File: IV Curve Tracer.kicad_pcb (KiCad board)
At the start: 2 copper layers, 159.4 x 80.1 mm, 61 parts, among them IC1 MAX680ESA+, J0 TB002-500-02BE, J1 CAN_Out, J5 Conn_01x15, J6 Conn_01x15, Q1 IRF100P218XKMA1, Q2 IRF100P218XKMA1, SW0 SW_Rotary2x3, U1 INA211CQDCKRQ1, U2 LT1215, U3 LT1215, U4 ADM3055E, U5 CDSOT23-T24CAN

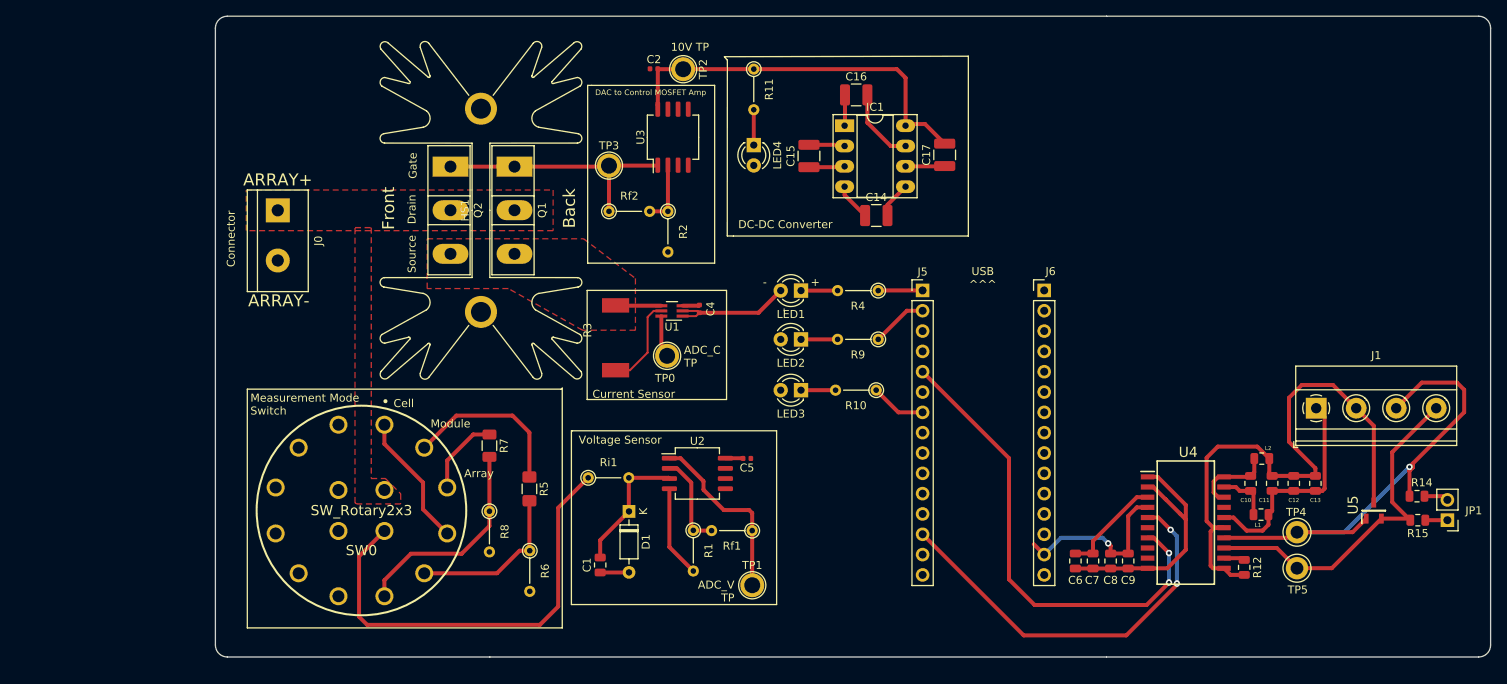
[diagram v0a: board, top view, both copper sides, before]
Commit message: CAN updated, needs bugfixes and footprint review.
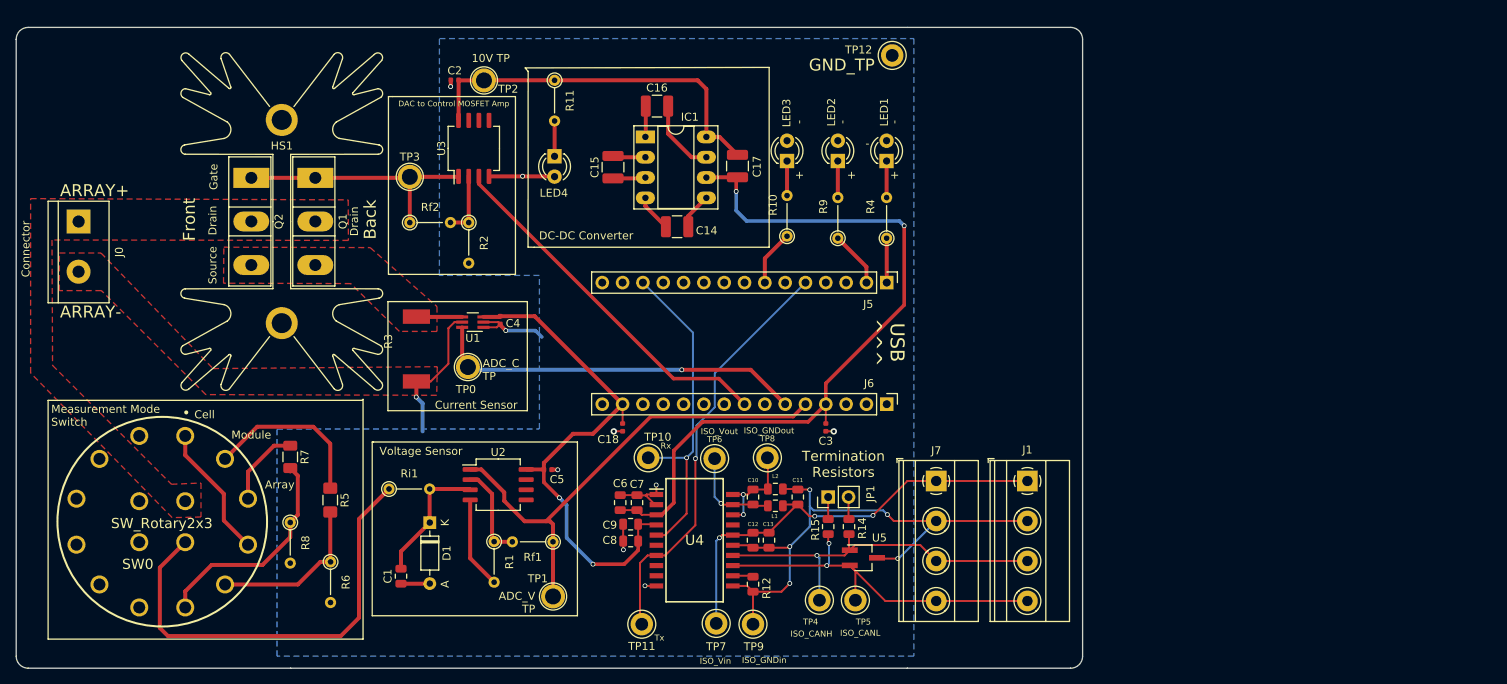
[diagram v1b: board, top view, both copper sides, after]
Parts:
- added C18: .1uF, Capacitor_SMD:C_0402_1005Metric, F.Cu at (171.5, 131.4)
- added C3: .1uF, Capacitor_SMD:C_0402_1005Metric, F.Cu at (196.9, 131.4)
- added J7: CAN_In, TerminalBlock_Phoenix:TerminalBlock_Phoenix_MKDS-1,5-4_1x04_P5.00mm_Horizontal, F.Cu at (210.7, 138.1)
- added TP10: CAN_Rx, TestPoint:TestPoint_Keystone_5005-5009_Compact, F.Cu at (174.7, 135.2)
- added TP11: CAN_Tx, TestPoint:TestPoint_Keystone_5005-5009_Compact, F.Cu at (173.9, 156.0)
- added TP12: GroundTP, TestPoint:TestPoint_Keystone_5005-5009_Compact, F.Cu at (205.2, 84.9)
- added TP6: ISO_Vout, TestPoint:TestPoint_Keystone_5005-5009_Compact, F.Cu at (183.0, 135.3)
- added TP7: ISO_Vin, TestPoint:TestPoint_Keystone_5005-5009_Compact, F.Cu at (183.2, 155.9)
- added TP8: ISO_GNDout, TestPoint:TestPoint_Keystone_5005-5009_Compact, F.Cu at (189.6, 135.2)
- added TP9: ISO_GNDin, TestPoint:TestPoint_Keystone_5005-5009_Compact, F.Cu at (187.8, 156.0)
- U5: footprint SamacSys_Parts:SOT95P230X117-3N -> Package_TO_SOT_SMD:SOT-23W_Handsoldering
- moved JP1 77.5 mm to (197.2, 140.1), turned to 90 degrees
- moved R15 73.7 mm to (197.2, 143.8), turned to 270 degrees
- moved R14 71.1 mm to (199.8, 143.8), turned to 270 degrees
- moved C13 68.7 mm to (189.8, 145.5), turned to 270 degrees
- moved C12 68.0 mm to (187.8, 145.5), turned to 270 degrees
- moved U5 64.1 mm to (201.6, 147.7), turned to 0 degrees
- moved C9 62.4 mm to (172.5, 143.5), turned to 180 degrees
- moved C10 62.2 mm to (187.8, 140.1)
- moved U4 61.4 mm to (180.5, 145.5)
- moved R12 61.4 mm to (187.8, 151.0)
- moved L2 60.9 mm to (190.6, 139.1)
- moved L1 60.7 mm to (190.6, 141.2)
- moved TP4 60.3 mm to (196.1, 153.0)
- moved C8 60.0 mm to (172.5, 145.6), turned to 180 degrees
- moved C11 59.3 mm to (193.4, 140.1)
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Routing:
- net +5V: track 17.8 -> 94.2 mm, vias 0 -> 2
- net DAC_Control: track 0.00 -> 45.6 mm
- net ADC_C: track 5.26 -> 46.8 mm, vias 0 -> 1
- net +3V3: track 26.5 -> 66.7 mm, vias 1 -> 2
- net ADC_V: track 22.8 -> 61.3 mm
- net Net-(C11-Pad1): track 28.1 -> 55.4 mm, vias 0 -> 3
- net /CAN_H: track 63.7 -> 46.0 mm
- net CAN_RX: track 50.4 -> 41.5 mm, vias 2 -> 1
- net CAN_TX: track 60.1 -> 52.6 mm, vias 2 -> 1
- net GND: track 79.9 -> 73.3 mm, vias 0 -> 10
- net Net-(C10-Pad1): track 6.64 -> 11.9 mm, vias 0 -> 1
- net /CAN_L: track 44.2 -> 47.4 mm, vias 0 -> 2
- net Net-(C10-Pad2): track 10.2 -> 12.5 mm, vias 0 -> 2
- net Net-(R7-Pad2): track 26.6 -> 27.9 mm
- net +10V: track 48.5 -> 47.6 mm
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- added copper zone on B.Cu, net GND
- added copper zone on F.Cu, net GND
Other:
- board size 159.4 x 80.1 mm -> 133.3 x 80.1 mm
- board text added: "A"
- board text added: "GND_TP"
- board text added: "ISO_CANH"
- board text added: "ISO_CANL"
- board text added: "ISO_GNDin"
- board text added: "ISO_GNDout"
- board text added: "ISO_Vin"
- board text added: "ISO_Vout"
- board text added: "Rx"
- board text added: "Termination Resistors"
- board text added: "Tx"

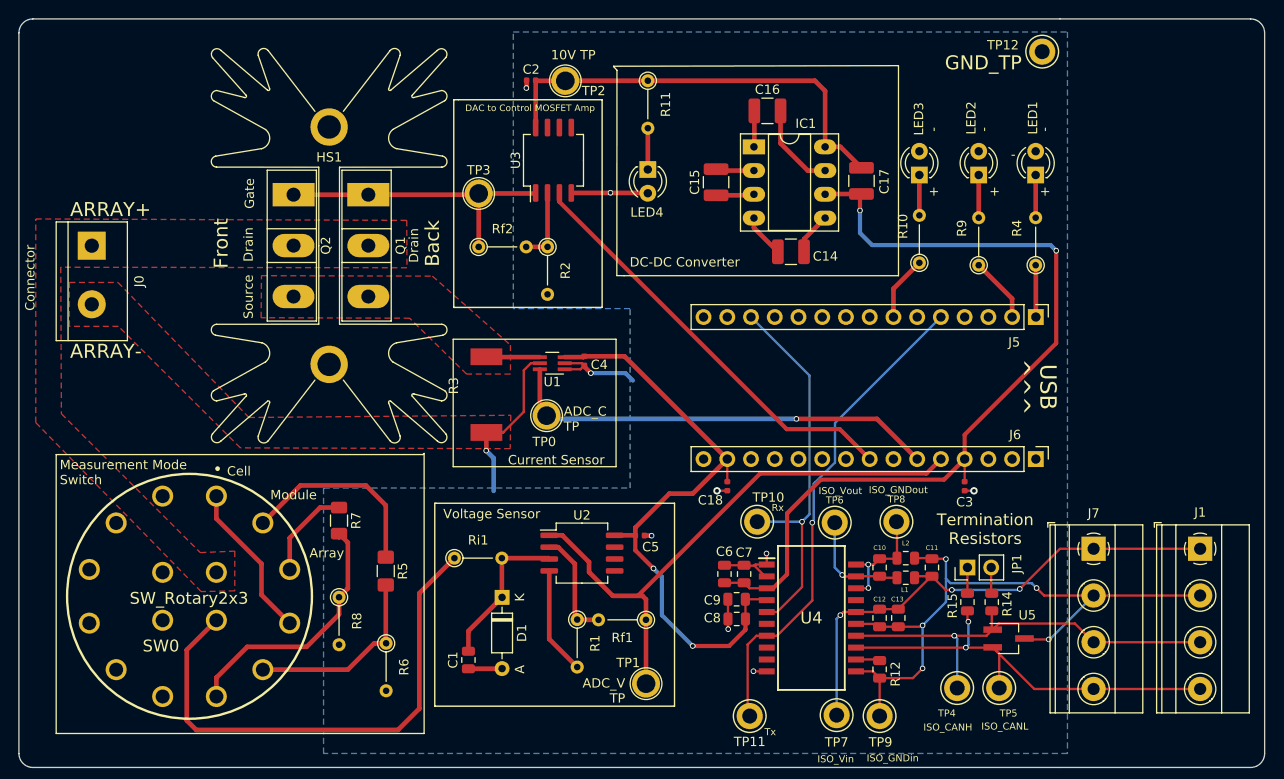
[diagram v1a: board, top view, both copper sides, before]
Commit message: proof checked, drc run and mounting holes added.
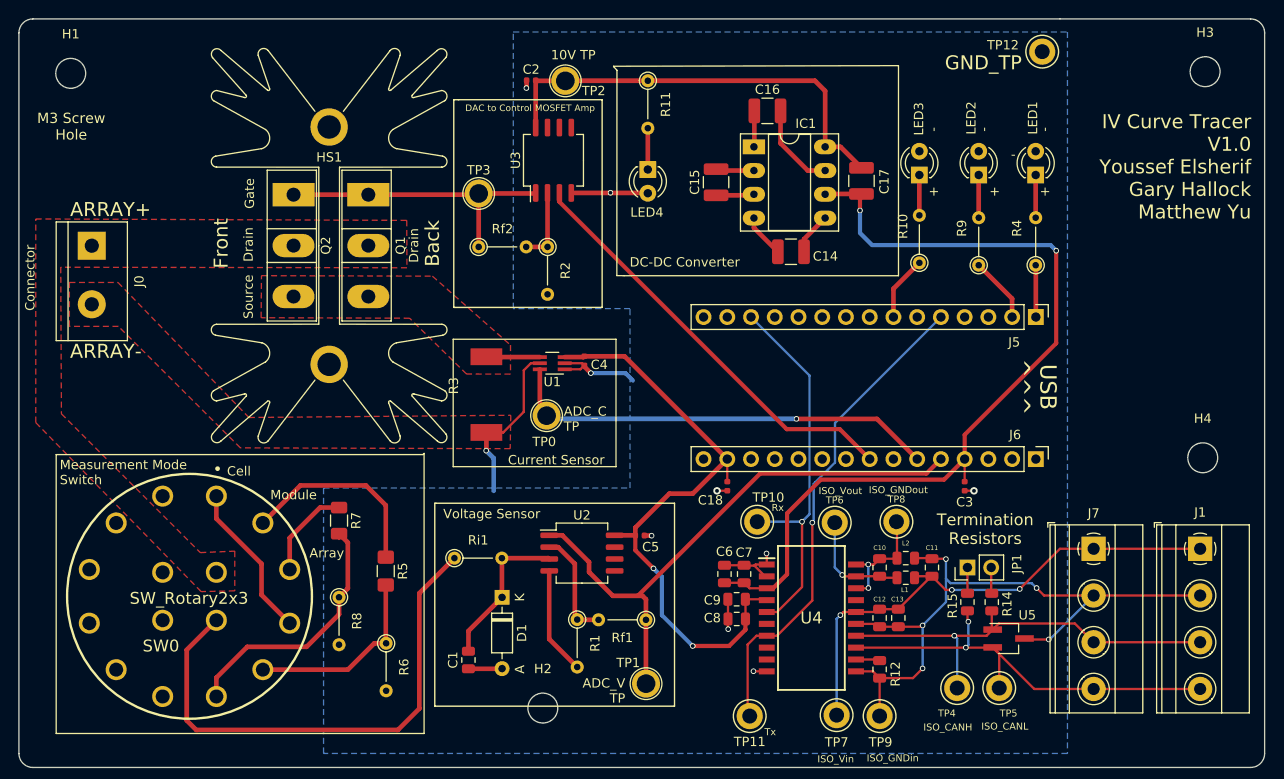
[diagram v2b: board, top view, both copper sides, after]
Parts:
- added H1: MountingHole, MountingHole:MountingHole_3.2mm_M3, F.Cu at (101.2, 87.2)
- added H2: MountingHole, MountingHole:MountingHole_3.2mm_M3, F.Cu at (151.8, 155.1)
- added H3: MountingHole, MountingHole:MountingHole_3.2mm_M3, F.Cu at (222.6, 87.0)
- added H4: MountingHole, MountingHole:MountingHole_3.2mm_M3, F.Cu at (222.4, 128.4)
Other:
- board text added: "IV Curve Tracer V1.0 Youssef Elsherif Gary Hallock Matthew Yu"
- board text added: "M3 Screw Hole"

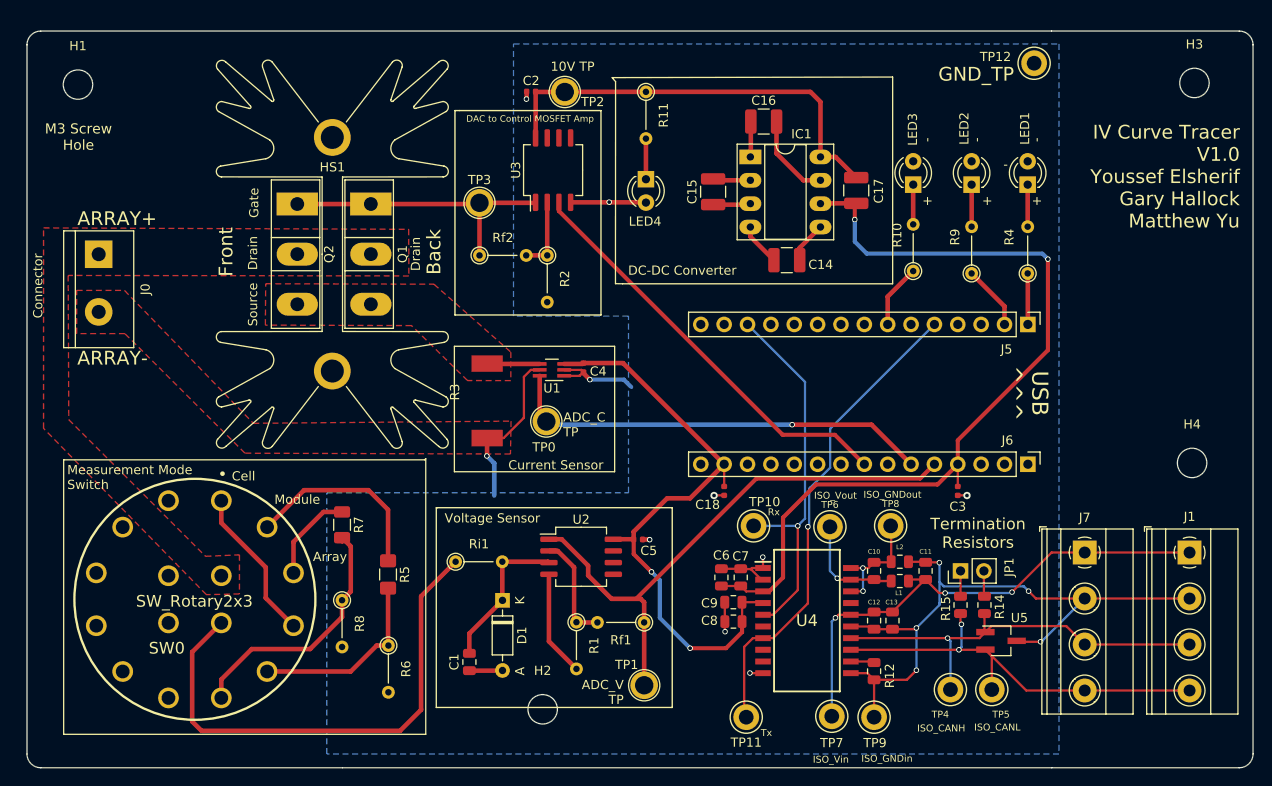
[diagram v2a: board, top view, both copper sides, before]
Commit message: rebuilt with MOSFET footprint flipped, traces rewired, and dot for every smd component where 1st pin is not obvious
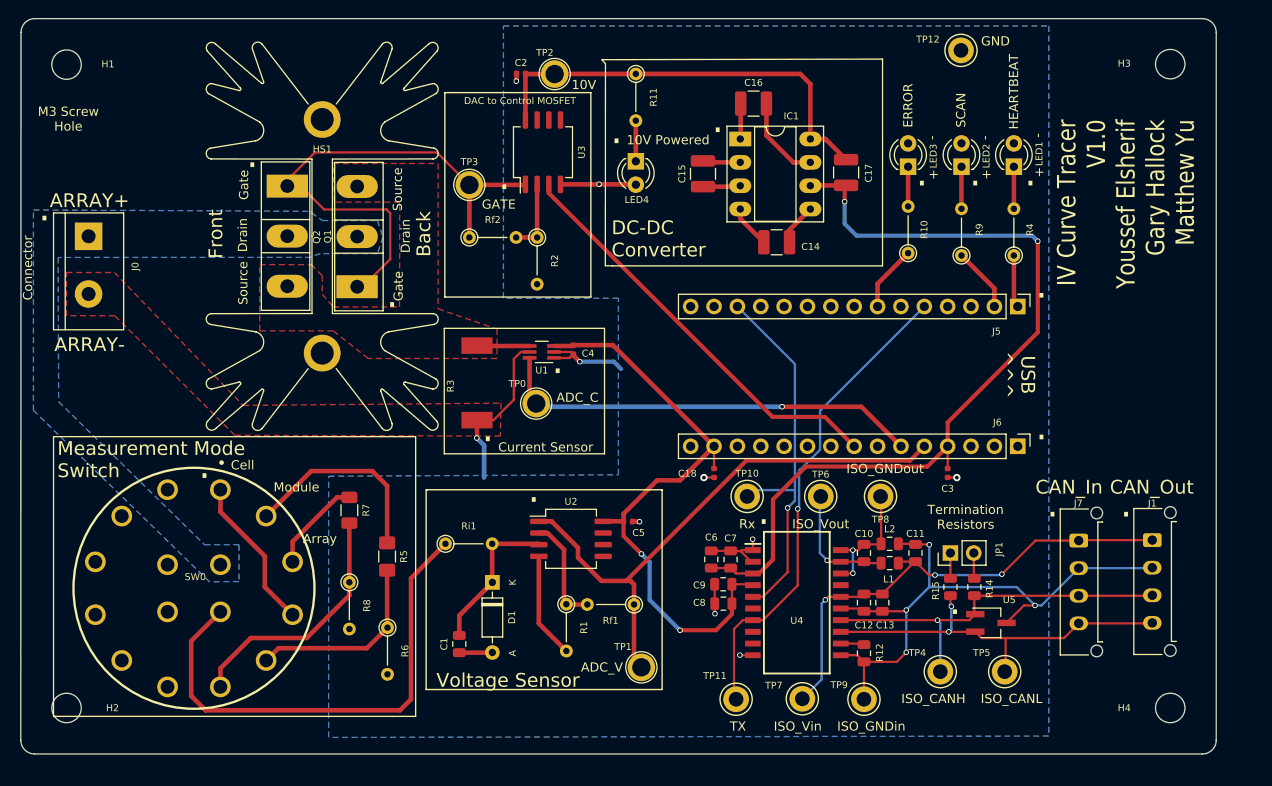
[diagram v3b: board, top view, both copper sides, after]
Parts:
- J1, J7: footprint TerminalBlock_Phoenix:TerminalBlock_Phoenix_MKDS-1,5-4_1x04_P5.00mm_Horizontal -> Connector_Molex:Molex_Micro-Fit_3.0_43650-0415_1x04_P3.00mm_Vertical
- moved H2 51.8 mm to (100.0, 155.0)
- moved H4 26.7 mm to (220.0, 155.0)
- moved Q1 9.12 mm to (131.6, 109.2), turned to 90 degrees
- moved TP12 8.07 mm to (197.2, 83.5)
- moved J1 4.27 mm to (218.1, 136.8)
- moved TP7 3.72 mm to (180.0, 154.0)
- moved TP6 3.45 mm to (182.0, 132.0)
- moved TP8 3.38 mm to (188.5, 132.0)
- moved H3 3.33 mm to (220.0, 85.0)
- moved TP10 3.28 mm to (174.0, 132.0)
- moved H1 2.50 mm to (100.0, 85.0)
- moved LED1 2.46 mm to (203.0, 96.2)
- moved R4 2.46 mm to (203.0, 105.8)
- moved TP5 2.40 mm to (202.0, 151.1)
- moved C7 2.24 mm to (172.2, 138.8)
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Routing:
- net GATE: track 31.7 -> 58.6 mm
- net Net-(C11-Pad2): track 72.7 -> 66.3 mm, vias 5 -> 4
- net /CAN_L: track 47.4 -> 43.2 mm
- net /CAN_H: track 46.0 -> 42.0 mm
- net Net-(C11-Pad1): track 55.4 -> 53.2 mm
- net Net-(Ri1-Pad1): track 55.9 -> 53.9 mm
- net Net-(C10-Pad1): track 11.9 -> 13.3 mm
- net Net-(C10-Pad2): track 12.5 -> 13.9 mm
- net Net-(R5-Pad1): track 21.2 -> 22.0 mm
- net Net-(R7-Pad2): track 27.9 -> 27.2 mm
- net CAN_RX: track 41.5 -> 42.2 mm
- added copper zone on B.Cu, net Net-(J0-Pad1)
- removed copper zone on F.Cu, net Net-(J0-Pad1)
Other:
- board size 133.3 x 80.1 mm -> 130 x 80 mm
- board text added: "."
- board text added: "10V"
- board text added: "10V Powered"
- board text added: "ADC_C"
- board text added: "ADC_V"
- board text added: "CAN_In"
- board text added: "CAN_Out"
- board text added: "DAC to Control MOSFET"
- board text added: "ERROR"
- board text added: "GATE"
- board text added: "GND"
- board text added: "HEARTBEAT"
- board text added: "SCAN"
- board text added: "TX"
- board text removed: "10V TP"
- board text removed: "ADC_C TP"
- board text removed: "ADC_V TP"
- board text removed: "DAC to Control MOSFET Amp"
- board text removed: "GND_TP"
- board text removed: "Tx"

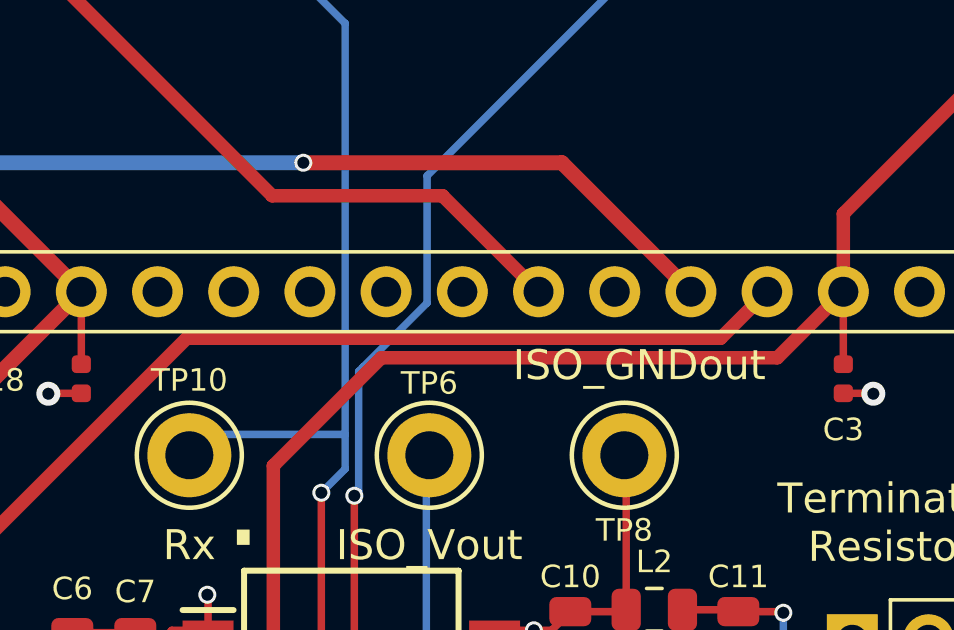
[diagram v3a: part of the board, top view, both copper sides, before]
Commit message: moved ADC_V pin down two
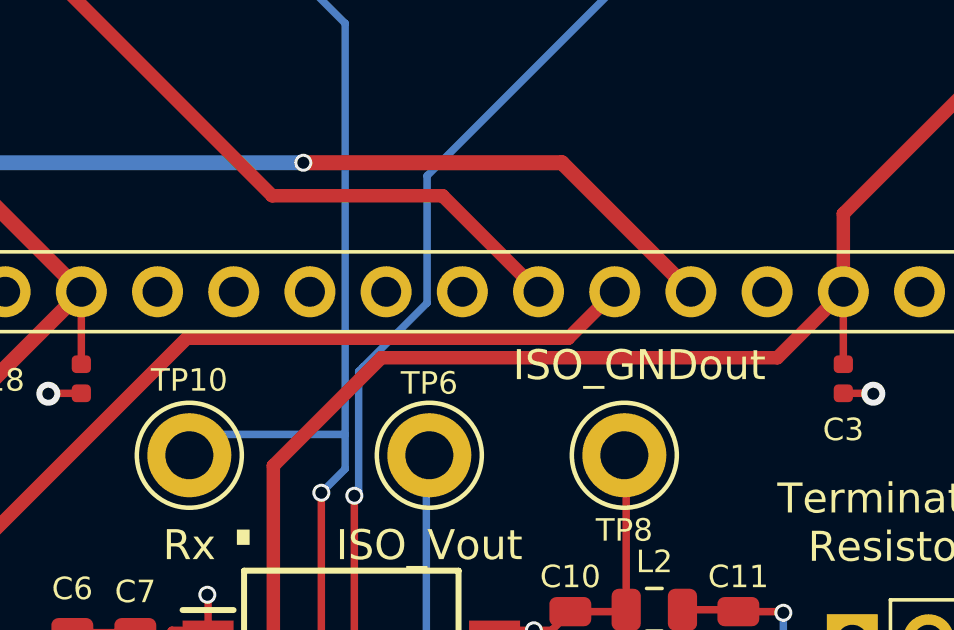
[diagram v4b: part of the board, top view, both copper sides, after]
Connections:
- J6 pad 5: ADC_V -> Net-(J6-Pad5)
- J6 pad 7: Net-(J6-Pad7) -> ADC_V
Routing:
- net ADC_V: track 61.7 -> 56.6 mm
